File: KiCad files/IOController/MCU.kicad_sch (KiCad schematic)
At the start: 8 parts, among them J1 AVR-ISP-6, J3 Conn_01x04, U1 AP7384-50SA, U2 ATtiny1634-M

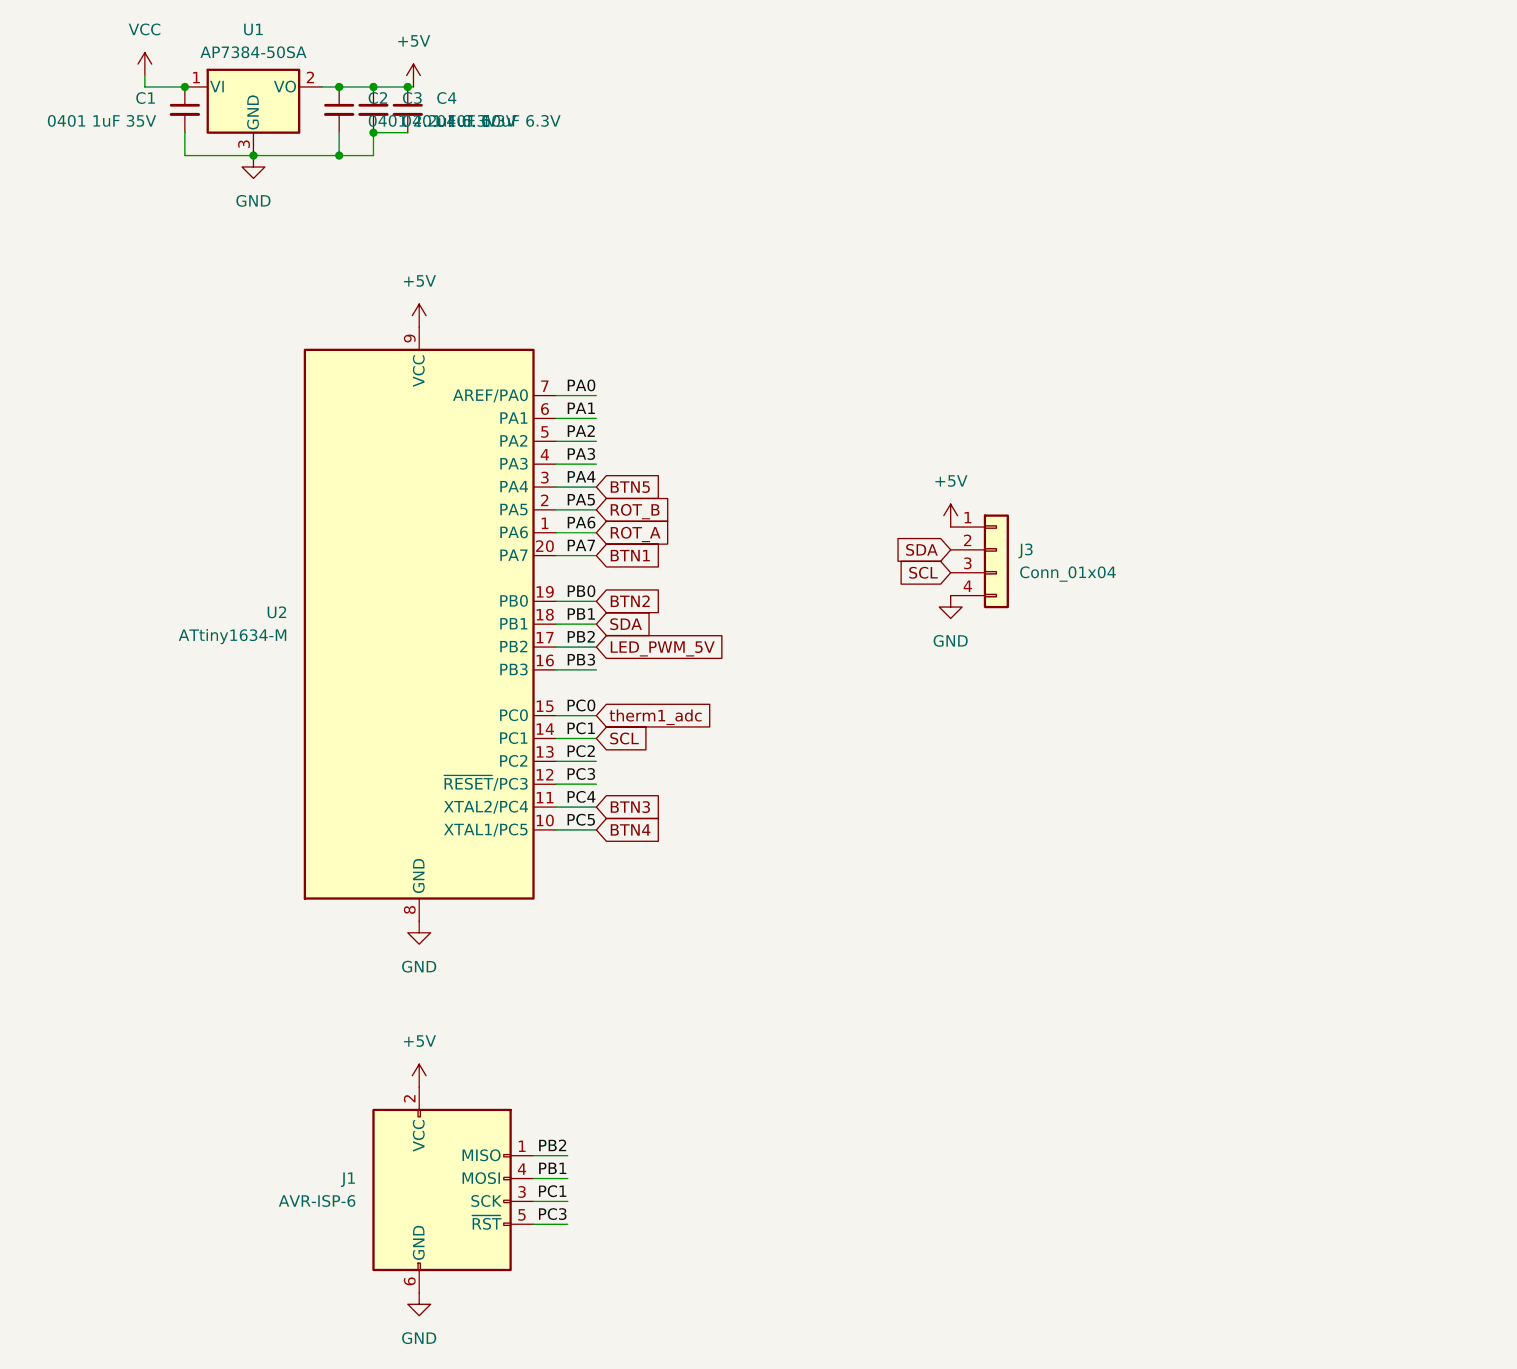
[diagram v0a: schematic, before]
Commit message: made some adjustments to improve design reliability.
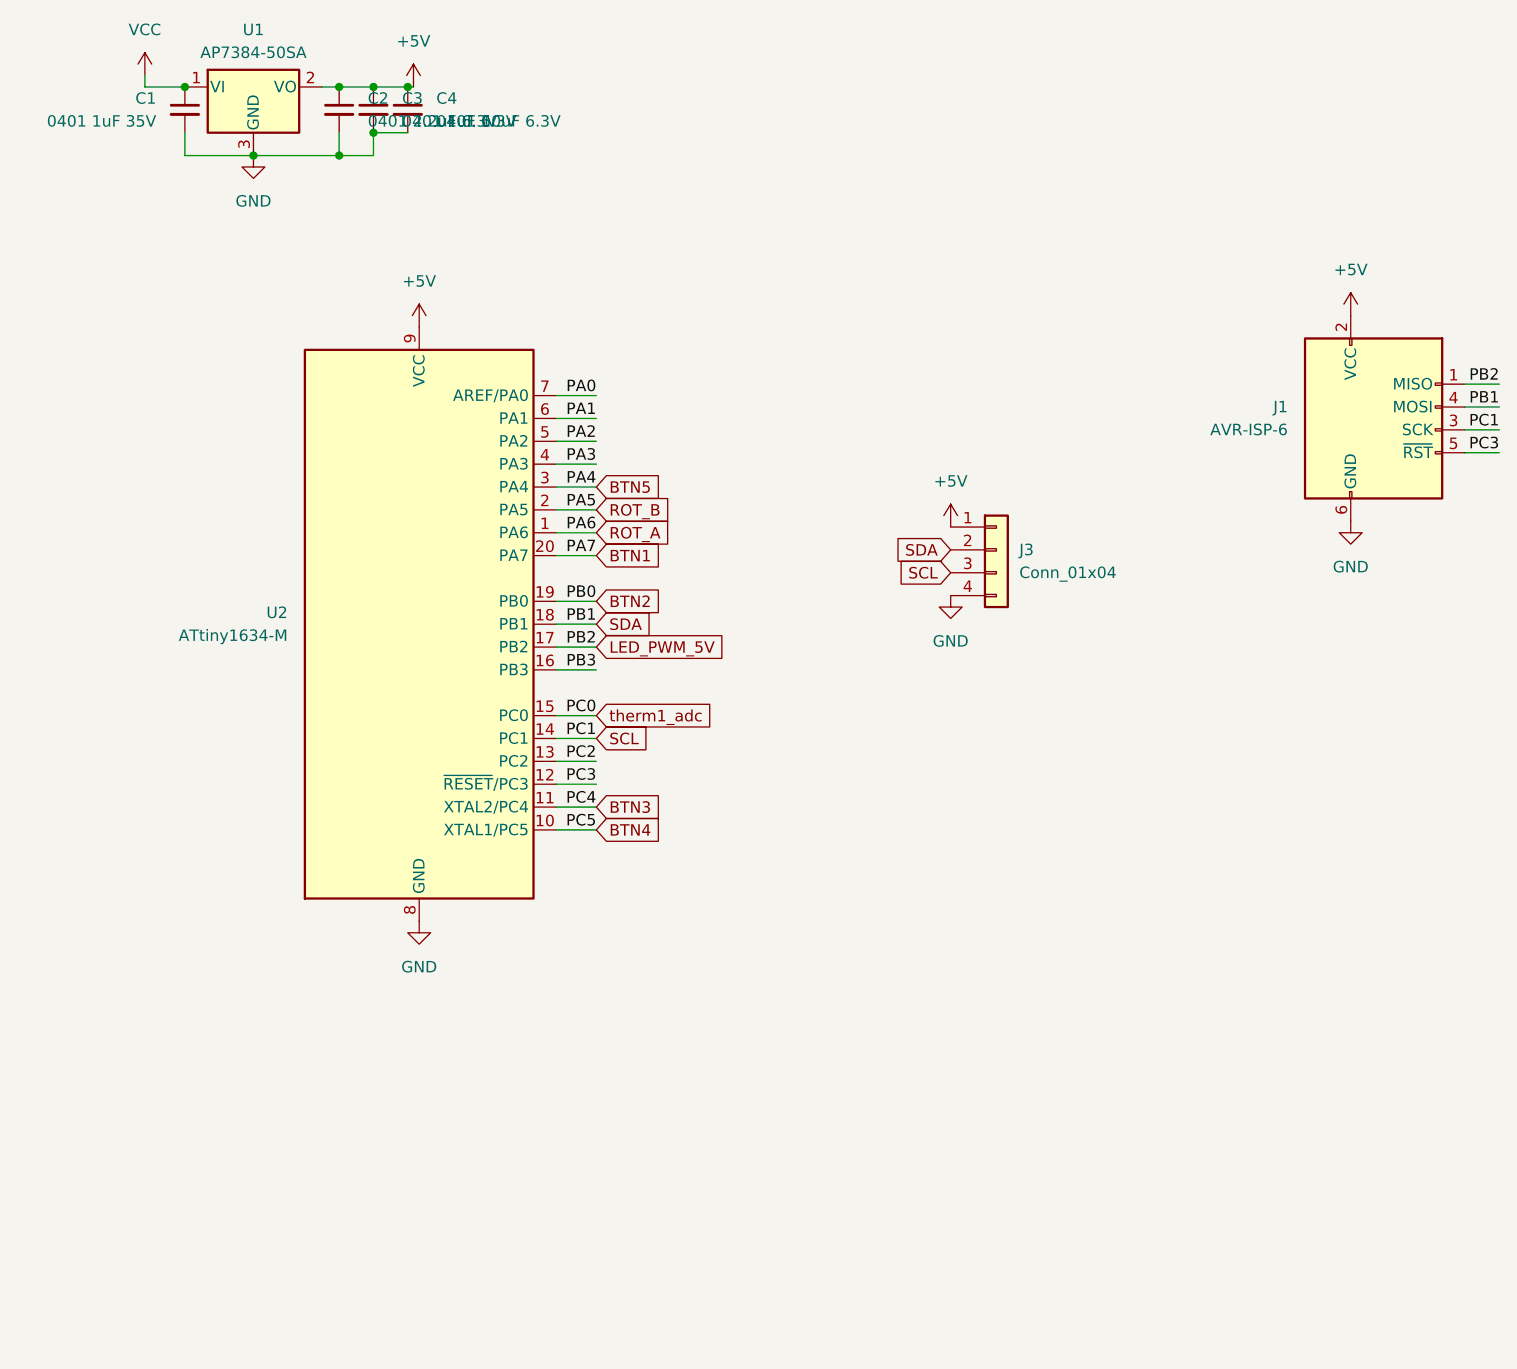
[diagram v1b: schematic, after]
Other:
- moved on the sheet: J1
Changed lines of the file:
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@@
 	(generator "eeschema")
 	(generator_version "8.0")
-	(paper "A3")
+	(paper "A5")
 	(junction
 		(at 30.48 20.955)
@@
 	(wire
 		(pts
-			(xy 73.025 147.32) (xy 69.215 147.32)
+			(xy 176.53 61.595) (xy 172.72 61.595)
 		)
 		(stroke
@@
 	(wire
 		(pts
-			(xy 73.025 142.24) (xy 69.215 142.24)
+			(xy 176.53 56.515) (xy 172.72 56.515)
 		)
 		(stroke
@@
 	(wire
 		(pts
-			(xy 73.025 139.7) (xy 69.215 139.7)
+			(xy 176.53 53.975) (xy 172.72 53.975)
 		)
 		(stroke
@@
 	(wire
 		(pts
-			(xy 73.025 144.78) (xy 69.215 144.78)
+			(xy 176.53 59.055) (xy 172.72 59.055)
 		)
 		(stroke
@@
 	)
 	(label "PC3"
-		(at 73.025 147.32 180)
+		(at 176.53 61.595 180)
 		(fields_autoplaced yes)
 		(effects
@@
 	)
 	(label "PB1"
-		(at 73.025 142.24 180)
+		(at 176.53 56.515 180)
 		(fields_autoplaced yes)
 		(effects
@@
 	)
 	(label "PB2"
-		(at 73.025 139.7 180)
+		(at 176.53 53.975 180)
 		(fields_autoplaced yes)
 		(effects
@@
 	)
 	(label "PC1"
-		(at 73.025 144.78 180)
+		(at 176.53 59.055 180)
 		(fields_autoplaced yes)
 		(effects
@@
 	(symbol
 		(lib_id "power:GND")
-		(at 56.515 154.94 0)
+		(at 160.02 69.215 0)
 		(unit 1)
 		(exclude_from_sim no)
@@
 		(fields_autoplaced yes)
 		(property "Reference" "#PWR07"
-			(at 56.515 161.29 0)
+			(at 160.02 75.565 0)
 			(effects
 				(font
@@
 		)
 		(property "Value" "GND"
-			(at 56.515 160.02 0)
+			(at 160.02 74.295 0)
 			(effects
 				(font
@@
 		)
 		(property "Footprint" ""
-			(at 56.515 154.94 0)
+			(at 160.02 69.215 0)
 			(effects
 				(font
@@
 		)
 		(property "Datasheet" ""
-			(at 56.515 154.94 0)
+			(at 160.02 69.215 0)
 			(effects
 				(font
@@
 		)
 		(property "Description" "Power symbol creates a global label with name \"GND\" , ground"
-			(at 56.515 154.94 0)
+			(at 160.02 69.215 0)
 			(effects
 				(font
@@
 	(symbol
 		(lib_id "Connector:AVR-ISP-6")
-		(at 59.055 144.78 0)
+		(at 162.56 59.055 0)
 		(unit 1)
 		(exclude_from_sim no)
@@
 		(fields_autoplaced yes)
 		(property "Reference" "J1"
-			(at 49.53 142.2399 0)
+			(at 153.035 56.5149 0)
 			(effects
 				(font
@@
 		)
 		(property "Value" "AVR-ISP-6"
-			(at 49.53 144.7799 0)
+			(at 153.035 59.0549 0)
 			(effects
 				(font
@@
 		)
 		(property "Footprint" "Connector_IDC:IDC-Header_2x03_P2.54mm_Vertical"
-			(at 52.705 143.51 90)
+			(at 156.21 57.785 90)
 			(effects
 				(font
@@
 		)
 		(property "Datasheet" "~"
-			(at 26.67 158.75 0)
+			(at 130.175 73.025 0)
 			(effects
 				(font
@@
 		)
 		(property "Description" "Atmel 6-pin ISP connector"
-			(at 59.055 144.78 0)
+			(at 162.56 59.055 0)
 			(effects
 				(font
@@
 	(symbol
 		(lib_id "power:+5V")
-		(at 56.515 132.08 0)
+		(at 160.02 46.355 0)
 		(unit 1)
 		(exclude_from_sim no)
@@
 		(fields_autoplaced yes)
 		(property "Reference" "#PWR06"
-			(at 56.515 135.89 0)
+			(at 160.02 50.165 0)
 			(effects
 				(font
@@
 		)
 		(property "Value" "+5V"
-			(at 56.515 127 0)
+			(at 160.02 41.275 0)
 			(effects
 				(font
@@
 		)
 		(property "Footprint" ""
-			(at 56.515 132.08 0)
+			(at 160.02 46.355 0)
 			(effects
 				(font
@@
 		)
 		(property "Datasheet" ""
-			(at 56.515 132.08 0)
+			(at 160.02 46.355 0)
 			(effects
 				(font
@@
 		)
 		(property "Description" "Power symbol creates a global label with name \"+5V\""
-			(at 56.515 132.08 0)
-			(effects
-				(font
+			(at 160.02 46.355 0)
+			(effects
+				(font
